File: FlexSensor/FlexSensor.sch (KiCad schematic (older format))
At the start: 160 parts

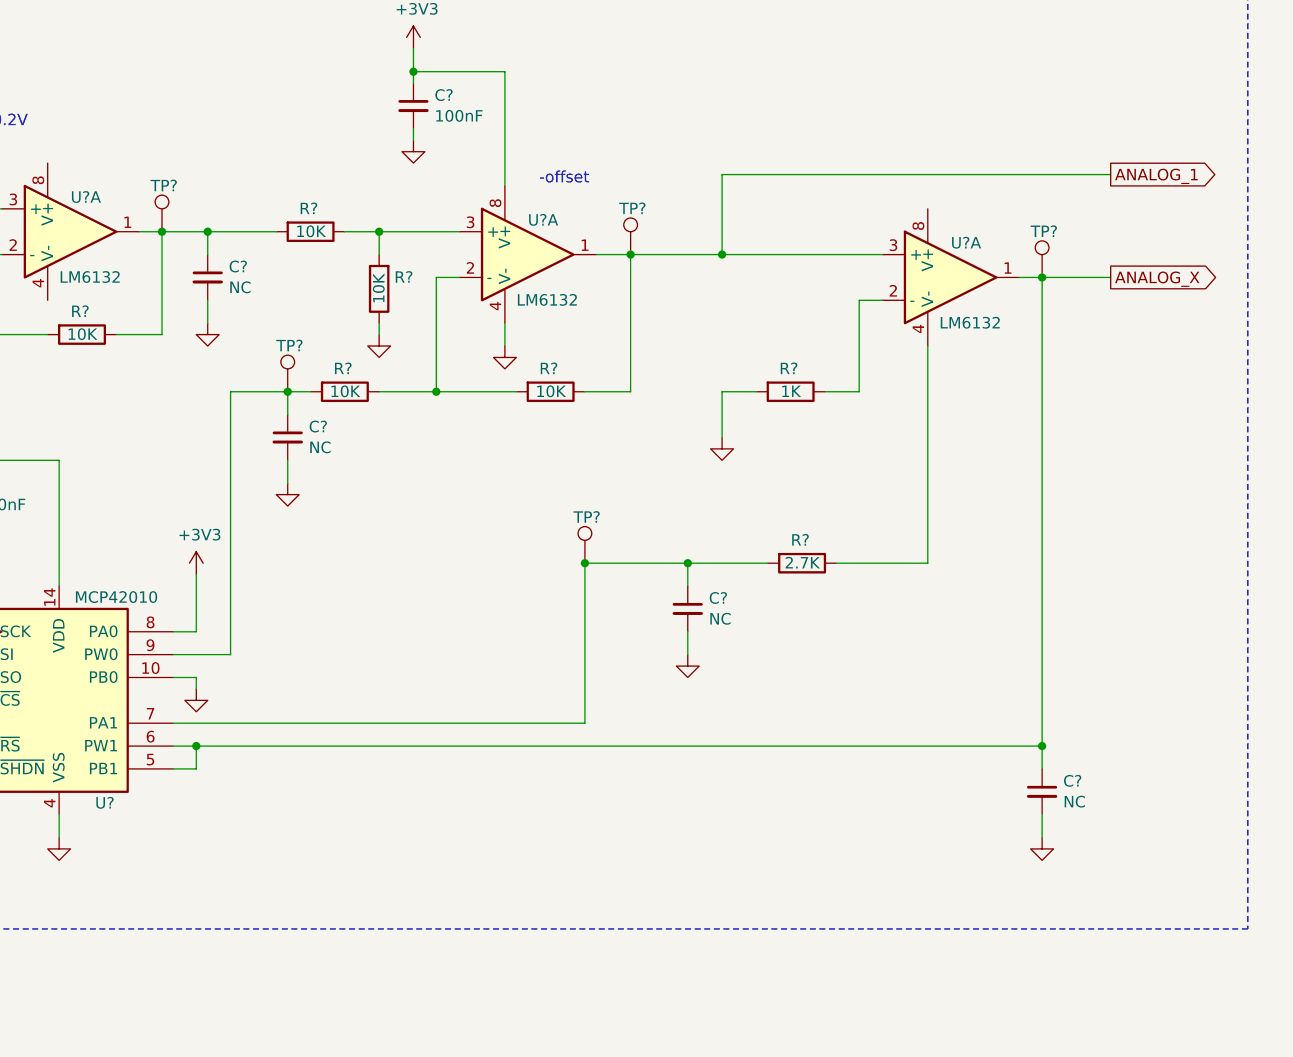
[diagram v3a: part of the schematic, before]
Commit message: Updated analog input path to be more flexible in amplification
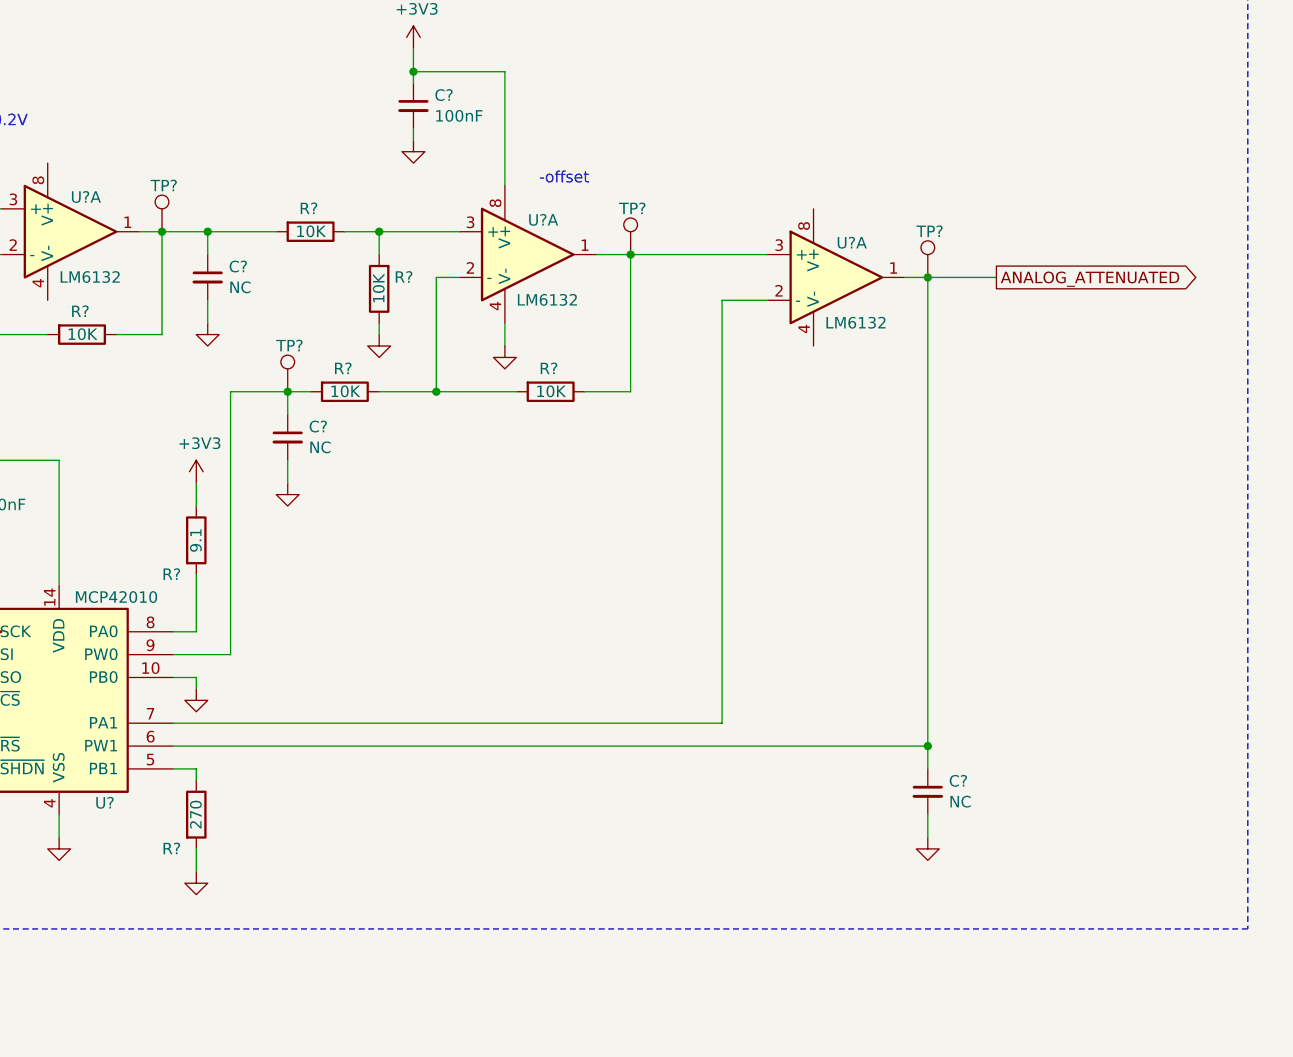
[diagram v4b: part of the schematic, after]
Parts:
- removed C?: NC, symbol Device:C_Small
- removed R?: 1K, symbol Device:R
- removed R?: 2.7K, symbol Device:R
- removed TP?: Test_Point, symbol Connector:Test_Point
- added R?: 9.1, symbol Device:R
- added R?: 270, symbol Device:R
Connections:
- net +3V3: now also R?.1; no longer U?.8 (PA0)
- net ANALOG_ATTENUATED: now also C?.1, TP?.1, U?.1, U?.6 (PW1)
- net GND: now also R?.2
- net at U?.7 (PA1): now also U?.2 (-)
- net ANALOG_1: no longer names the net of R?.1, TP?.1, U?.1, U?.3 (+)
- removed net ANALOG_X: C?.1, TP?.1, U?.1, U?.5 (PB1), U?.6 (PW1)
- new net: R?.2, U?.8 (PA0)
- new net: R?.1, U?.5 (PB1)
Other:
- moved on the sheet: C?, TP?, U?A
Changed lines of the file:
@@
 	1    0    0    -1
 $EndComp
-Text GLabel 20650 21100 2    50   Output ~ 0
-ANALOG_1
 Wire Wire Line
 	13200 21050 13200 21150
@@
 L Amplifier_Operational:LM358 U?
 U 1 1 5D52D9E1
-P 19950 21550
-F 0 "U?" H 19950 21700 50  0000 L CNN
-F 1 "LM6132" H 19900 21350 50  0000 L CNN
-F 2 "" H 19950 21550 50  0001 C CNN
-F 3 "http://www.ti.com/lit/ds/symlink/lm358.pdf" H 19950 21550 50  0001 C CNN
-	1    19950 21550
+P 19450 21550
+F 0 "U?" H 19450 21700 50  0000 L CNN
+F 1 "LM6132" H 19400 21350 50  0000 L CNN
+F 2 "" H 19450 21550 50  0001 C CNN
+F 3 "http://www.ti.com/lit/ds/symlink/lm358.pdf" H 19450 21550 50  0001 C CNN
+	1    19450 21550
 	1    0    0    -1
 $EndComp
@@
 	17050 22050 17150 22050
 Wire Wire Line
-	20650 21100 18950 21100
-Wire Wire Line
-	18950 21100 18950 21450
-Wire Wire Line
-	18950 21450 19650 21450
-Connection ~ 18950 21450
-Wire Wire Line
-	20350 21550 20250 21550
-Wire Wire Line
-	19550 22050 19550 21650
-Wire Wire Line
-	19550 21650 19650 21650
-$Comp
-L Device:R R?
-U 1 1 5E2AF3FC
-P 19250 22050
-F 0 "R?" V 19150 22000 50  0000 L CNN
-F 1 "1K" V 19250 22050 50  0000 C CNN
-F 2 "" V 19180 22050 50  0001 C CNN
-F 3 "~" H 19250 22050 50  0001 C CNN
-	1    19250 22050
-	0    1    1    0
-$EndComp
-Wire Wire Line
-	19400 22050 19550 22050
-Wire Wire Line
-	19100 22050 18950 22050
-Wire Wire Line
-	18950 22050 18950 22250
-$Comp
-L power:GND #PWR?
-U 1 1 5E35C73F
-P 18950 22250
-F 0 "#PWR?" H 18950 22000 50  0001 C CNN
-F 1 "GND" H 19100 22200 50  0001 C TNN
-F 2 "" H 18950 22250 50  0001 C CNN
-F 3 "" H 18950 22250 50  0001 C CNN
-	1    18950 22250
-	1    0    0    -1
-$EndComp
+	19850 21550 19750 21550
 $Comp
 L Connector:Test_Point TP?
 U 1 1 5E35C8AA
-P 20350 21550
-F 0 "TP?" H 20300 21750 50  0000 L CNN
-F 1 "Test_Point" H 20408 21579 50  0001 L CNN
-F 2 "" H 20550 21550 50  0001 C CNN
-F 3 "~" H 20550 21550 50  0001 C CNN
-	1    20350 21550
+P 19850 21550
+F 0 "TP?" H 19800 21750 50  0000 L CNN
+F 1 "Test_Point" H 19908 21579 50  0001 L CNN
+F 2 "" H 20050 21550 50  0001 C CNN
+F 3 "~" H 20050 21550 50  0001 C CNN
+	1    19850 21550
 	1    0    0    -1
 $EndComp
-Connection ~ 20350 21550
-Wire Wire Line
-	18550 21450 18950 21450
+Connection ~ 19850 21550
 Wire Wire Line
-	20350 23900 20350 24000
+	19850 23900 19850 24000
 $Comp
 L power:GND #PWR?
 U 1 1 5E3B3697
-P 20350 24000
-F 0 "#PWR?" H 20350 23750 50  0001 C CNN
-F 1 "GND" H 20500 23950 50  0001 C TNN
-F 2 "" H 20350 24000 50  0001 C CNN
-F 3 "" H 20350 24000 50  0001 C CNN
-	1    20350 24000
+P 19850 24000
+F 0 "#PWR?" H 19850 23750 50  0001 C CNN
+F 1 "GND" H 20000 23950 50  0001 C TNN
+F 2 "" H 19850 24000 50  0001 C CNN
+F 3 "" H 19850 24000 50  0001 C CNN
+	1    19850 24000
 	1    0    0    -1
 $EndComp
 Wire Wire Line
-	20350 21550 20650 21550
+	19850 21550 20150 21550
 Wire Notes Line
 	12400 19850 21250 19850
@@
 Wire Wire Line
 	16800 22050 17050 22050
-Wire Wire Line
-	20350 21550 20350 23600
-Text GLabel 20650 21550 2    50   Output ~ 0
-ANALOG_X
-Wire Wire Line
-	19850 21850 19850 22800
-$Comp
-L Device:R R?
-U 1 1 5E585B3E
-P 19300 22800
-F 0 "R?" V 19200 22750 50  0000 L CNN
-F 1 "2.7K" V 19300 22800 50  0000 C CNN
-F 2 "" V 19230 22800 50  0001 C CNN
-F 3 "~" H 19300 22800 50  0001 C CNN
-	1    19300 22800
-	0    1    1    0
-$EndComp
-Wire Wire Line
-	19450 22800 19850 22800
-Wire Wire Line
-	19150 22800 18800 22800
-Wire Wire Line
-	18350 22800 18350 23500
+Text GLabel 20150 21550 2    50   Output ~ 0
+ANALOG_ATTENUATED
 $Comp
 L Device:C_Small C?
@@
 $Comp
 L Device:C_Small C?
-U 1 1 5E70252B
-P 18800 23000
-F 0 "C?" H 18892 23046 50  0000 L CNN
-F 1 "NC" H 18892 22955 50  0000 L CNN
-F 2 "" H 18800 23000 50  0001 C CNN
-F 3 "~" H 18800 23000 50  0001 C CNN
-	1    18800 23000
-	1    0    0    -1
-$EndComp
-Wire Wire Line
-	18800 22800 18800 22900
-Wire Wire Line
-	18800 23100 18800 23200
-$Comp
-L power:GND #PWR?
-U 1 1 5E702533
-P 18800 23200
-F 0 "#PWR?" H 18800 22950 50  0001 C CNN
-F 1 "GND" H 18950 23150 50  0001 C TNN
-F 2 "" H 18800 23200 50  0001 C CNN
-F 3 "" H 18800 23200 50  0001 C CNN
-	1    18800 23200
-	1    0    0    -1
-$EndComp
-$Comp
-L Connector:Test_Point TP?
-U 1 1 5E7822B9
-P 18350 22800
-F 0 "TP?" H 18300 23000 50  0000 L CNN
-F 1 "Test_Point" H 18408 22829 50  0001 L CNN
-F 2 "" H 18550 22800 50  0001 C CNN
-F 3 "~" H 18550 22800 50  0001 C CNN
-	1    18350 22800
-	1    0    0    -1
-$EndComp
-Connection ~ 18350 22800
-Connection ~ 18800 22800
-Wire Wire Line
-	18800 22800 18350 22800
-Wire Wire Line
-	16550 23500 18350 23500
-$Comp
-L Device:C_Small C?
 U 1 1 5E88261D
-P 20350 23800
-F 0 "C?" H 20442 23846 50  0000 L CNN
-F 1 "NC" H 20442 23755 50  0000 L CNN
-F 2 "" H 20350 23800 50  0001 C CNN
-F 3 "~" H 20350 23800 50  0001 C CNN
-	1    20350 23800
+P 19850 23800
+F 0 "C?" H 19942 23846 50  0000 L CNN
+F 1 "NC" H 19942 23755 50  0000 L CNN
+F 2 "" H 19850 23800 50  0001 C CNN
+F 3 "~" H 19850 23800 50  0001 C CNN
+	1    19850 23800
 	1    0    0    -1
 $EndComp
 Wire Wire Line
-	16550 23600 16650 23600
-Connection ~ 20350 23600
-Wire Wire Line
-	20350 23600 20350 23700
-Wire Wire Line
 	16550 23700 16650 23700
 Wire Wire Line
-	16650 23700 16650 23600
-Connection ~ 16650 23600
-Wire Wire Line
-	16650 23600 20350 23600
-Wire Wire Line
 	17450 21350 17450 21450
 Connection ~ 17450 21350
@@
 L power:+3V3 #PWR?
 U 1 1 5E086E92
-P 16650 22850
-F 0 "#PWR?" H 16650 22700 50  0001 C CNN
-F 1 "+3V3" H 16665 23023 50  0000 C CNN
-F 2 "" H 16650 22850 50  0001 C CNN
-F 3 "" H 16650 22850 50  0001 C CNN
-	1    16650 22850
+P 16650 22450
+F 0 "#PWR?" H 16650 22300 50  0001 C CNN
+F 1 "+3V3" H 16665 22623 50  0000 C CNN
+F 2 "" H 16650 22450 50  0001 C CNN
+F 3 "" H 16650 22450 50  0001 C CNN
+	1    16650 22450
 	1    0    0    -1
 $EndComp
@@
 	1    0    0    -1
 $EndComp
+Wire Wire Line
+	19850 21550 19850 23600
+Wire Wire Line
+	18950 23500 18950 21650
+Wire Wire Line
+	18950 21650 19150 21650
+Wire Wire Line
+	16550 23500 18950 23500
+Wire Wire Line
+	16550 23600 19850 23600
+Connection ~ 19850 23600
+Wire Wire Line
+	19850 23600 19850 23700
+Wire Wire Line
+	16650 23700 16650 23750
+$Comp
+L power:GND #PWR?
+U 1 1 5B97B651
+P 16650 24150
+F 0 "#PWR?" H 16650 23900 50  0001 C CNN
+F 1 "GND" H 16655 23977 50  0001 C CNN
+F 2 "" H 16650 24150 50  0001 C CNN
+F 3 "" H 16650 24150 50  0001 C CNN
+	1    16650 24150
+	1    0    0    -1
+$EndComp
+Wire Wire Line
+	18550 21450 19150 21450
+$Comp
+L Device:R R?
+U 1 1 5B0717F3
+P 16650 22700
+F 0 "R?" H 16500 22550 50  0000 L CNN
+F 1 "9.1" V 16650 22700 50  0000 C CNN
+F 2 "" V 16580 22700 50  0001 C CNN
+F 3 "~" H 16650 22700 50  0001 C CNN
+	1    16650 22700
+	1    0    0    -1
+$EndComp
+Wire Wire Line
+	16650 22550 16650 22450
+$Comp
+L Device:R R?
+U 1 1 5B112EDA
+P 16650 23900
+F 0 "R?" H 16500 23750 50  0000 L CNN
+F 1 "270" V 16650 23900 50  0000 C CNN
+F 2 "" V 16580 23900 50  0001 C CNN
+F 3 "~" H 16650 23900 50  0001 C CNN
+	1    16650 23900
+	1    0    0    -1
+$EndComp
+Wire Wire Line
+	16650 24150 16650 24050
 Wire Bus Line
 	3350 14400 4950 14400

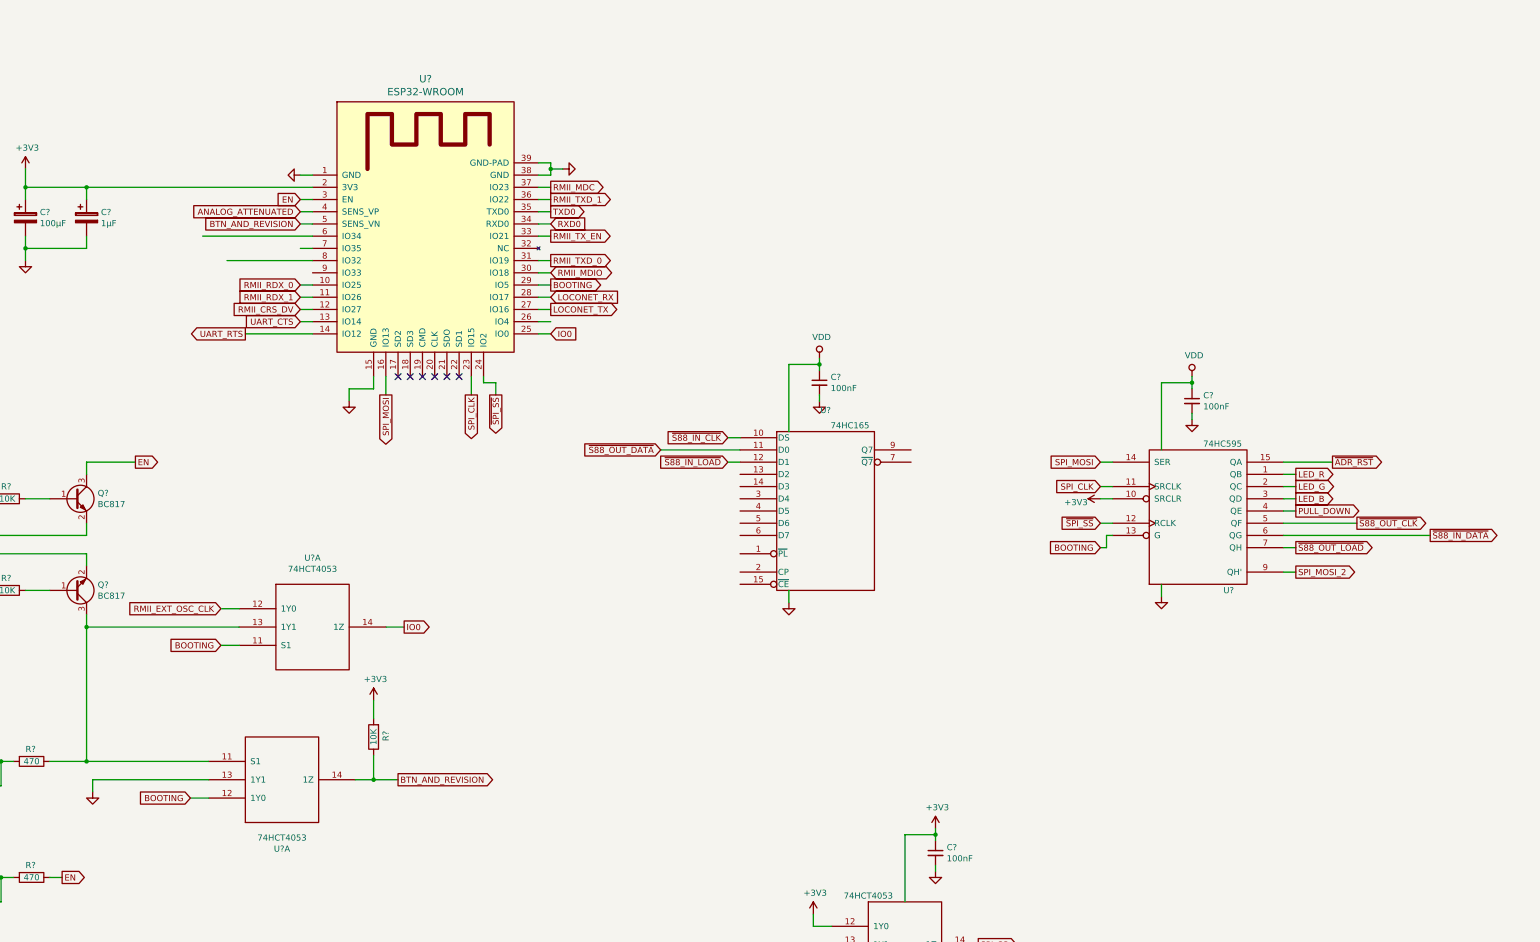
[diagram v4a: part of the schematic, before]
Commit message: Added XPRESS net pins on the ESP32. Still looking for a way to control input address
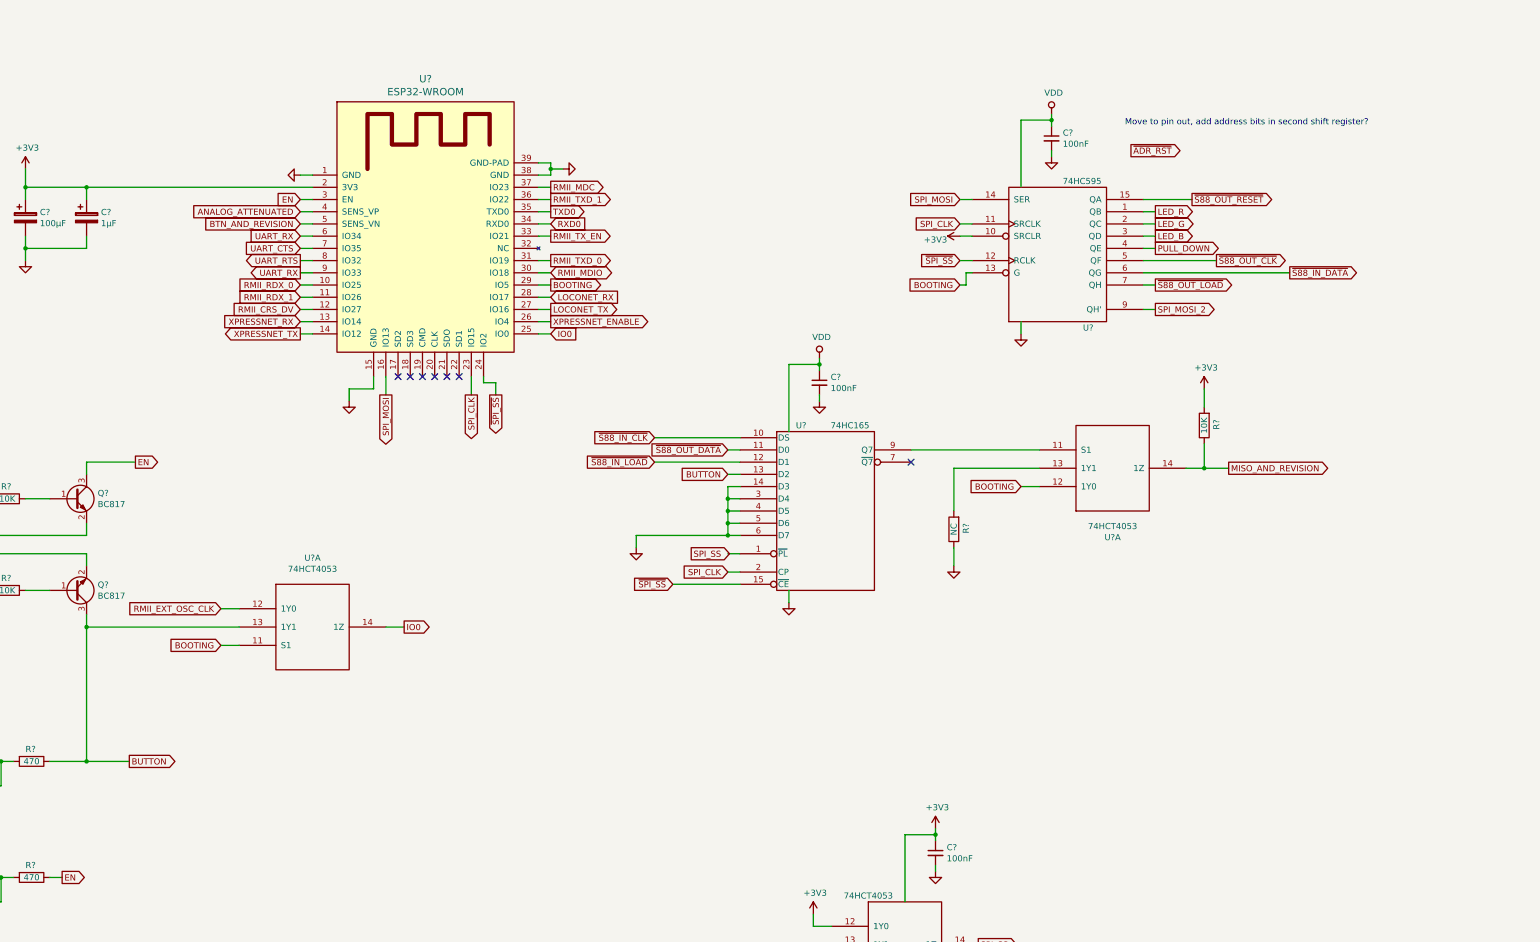
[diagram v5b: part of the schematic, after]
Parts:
- added R?: NC, symbol Device:R
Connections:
- net BTN_AND_REVISION: no longer R?.1, U?.14 (1Z)
- net GND: now also U?.14 (D3), U?.3 (D4), U?.4 (D5), U?.5 (D6), U?.6 (D7), R?.1; no longer U?.13 (1Y1)
- net SPI_CLK: now also U?.2 (CP)
- net UART_CTS: now also U?.7 (IO35); no longer U?.13 (IO14)
- net UART_RTS: now also U?.8 (IO32); no longer U?.14 (IO12)
- net ~ADR_RST: no longer U?.15 (QA)
- net ~S88_OUT_RESET: now also U?.15 (QA)
- net ~SPI_SS: now also U?.15 (~CE)
- net XPRESSNET_ENABLE: now reaches U?.26 (IO4)
- net UART_RX: now reaches U?.6 (IO34)
- net UART_RX: now also U?.9 (IO33)
- net BUTTON: now reaches U?.13 (D2)
- net BUTTON: now also Q?.3 (C), R?.1, U?.13 (1Y1)
- net at U?.9 (Q7): now also U?.11 (S1)
- new net: R?.2, U?.13 (1Y1)
- new net MISO_AND_REVISION: R?.1, U?.14 (1Z)
- new net XPRESSNET_RX: U?.13 (IO14)
- new net XPRESSNET_TX: U?.14 (IO12)
- no-connect marks 15 -> 16
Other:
- note added: "Move to pin out, add address bits in second shift register?"
- moved on the sheet: C?, R?, U?, U?A
